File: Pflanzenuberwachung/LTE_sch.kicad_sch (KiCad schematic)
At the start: 0 parts

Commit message: Bauteile in KI CAD importiert
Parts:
- added IC1: 2615011136000, 2615011136000, symbol Bauteile:2615011136000
- added J1: Antennen Anschluss, Bauteile:Antennen Anschluss, symbol Bauteile:Antennen Anschluss
- added J2: Nano Sim, Bauteile:Nano Sim, symbol Bauteile:Nano Sim

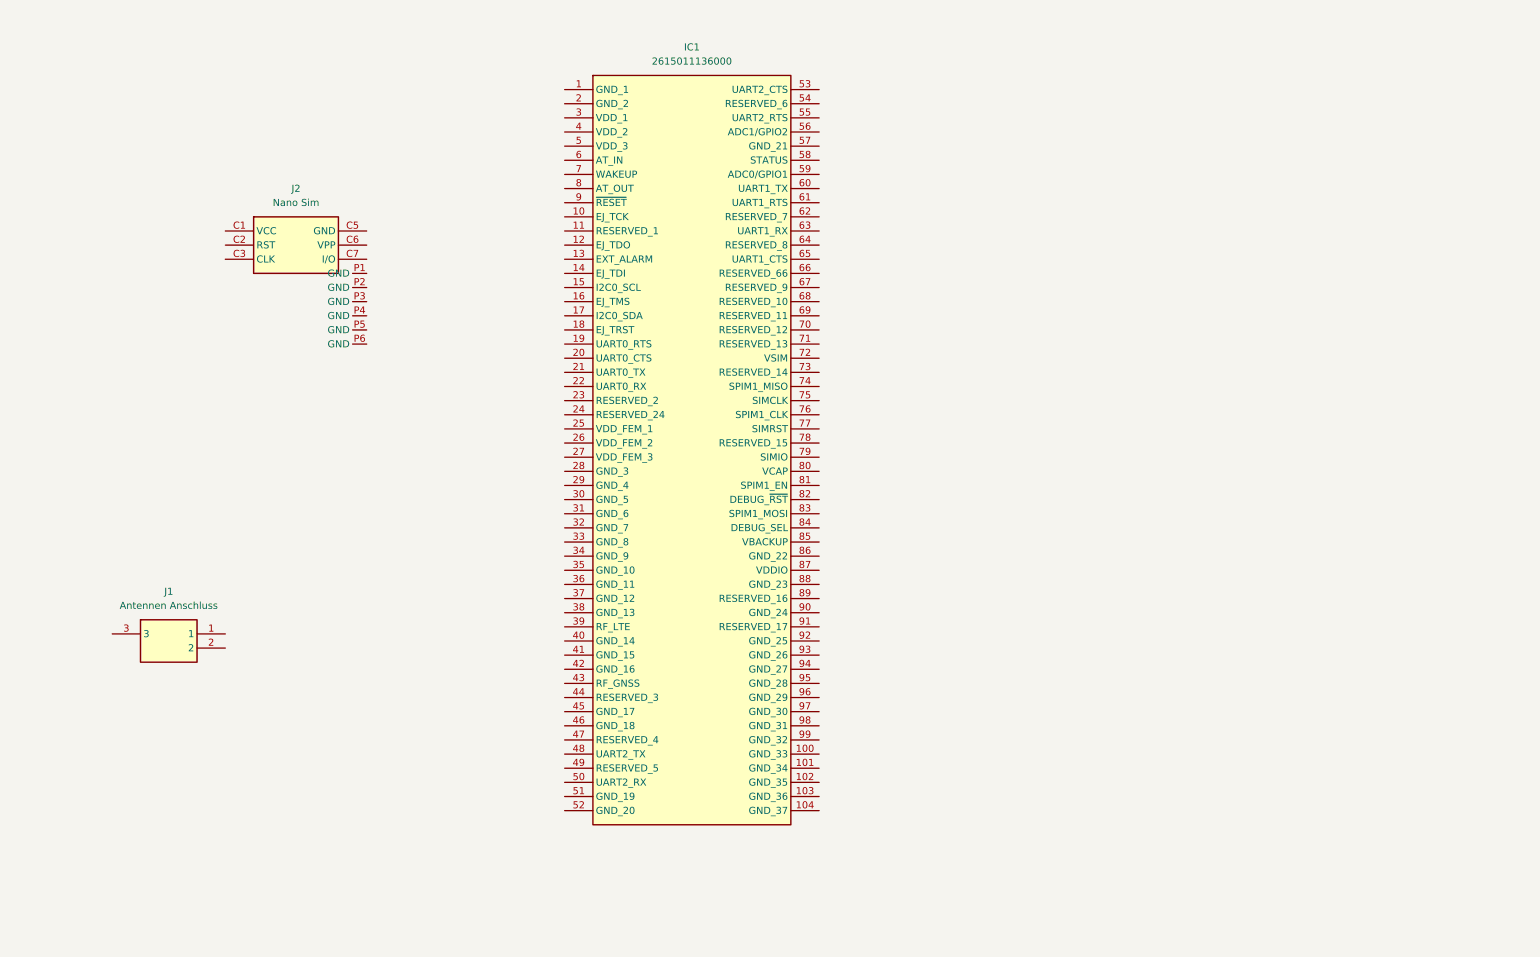
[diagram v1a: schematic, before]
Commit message: LTE und Sensoren
LTE modul und Ausgänge für Sensoren hinzugefügt
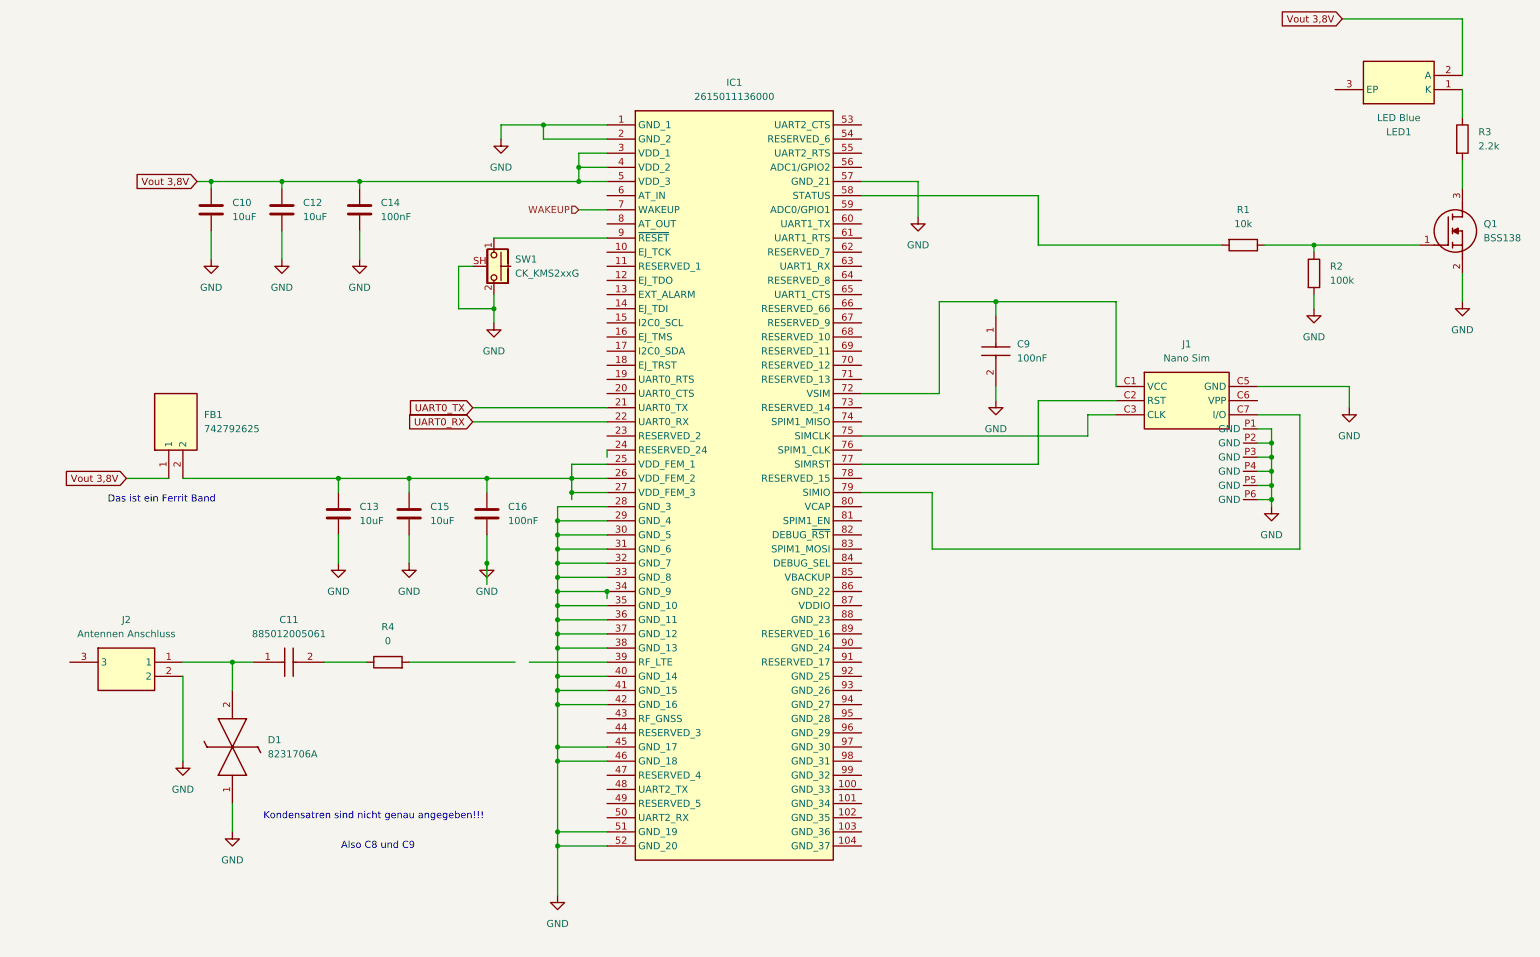
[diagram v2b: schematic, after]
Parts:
- removed J1: Antennen Anschluss, Bauteile:Antennen Anschluss, symbol Bauteile:Antennen Anschluss
- removed J2: Nano Sim, Bauteile:Nano Sim, symbol Bauteile:Nano Sim
- added C10, C12, C13, C15: 10uF, Capacitor_SMD:C_0805_2012Metric, symbol Device:C
- added C11: 885012005061, CAPC1005X55N, symbol Bauteile2:885012005061
- added C14, C16: 100nF, Capacitor_SMD:C_0805_2012Metric, symbol Device:C
- added C9: 100nF, Capacitor_SMD:C_0805_2012Metric, symbol Bauteile2:885012205037
- added D1: 8231706A, DIONC1005X60N, symbol Bauteile2:8231706A
- added FB1: 742792625, BEADC1608X100N, symbol Bauteile2:742792625
- added J1: Nano Sim, Bauteile:Nano Sim, symbol Bauteile:Nano Sim
- added J2: Antennen Anschluss, Bauteile:Antennen Anschluss, symbol Bauteile:Antennen Anschluss
- added LED1: LED Blue, Bauteile:LED Blue, symbol Bauteile:LED Blue
- added Q1: BSS138, Bauteile:Mosfed BSS138, symbol Bauteile:BSS138
- added R1: 10k, Resistor_SMD:R_0805_2012Metric, symbol Device:R
- added R2: 100k, Resistor_SMD:R_0805_2012Metric, symbol Device:R
- added R3: 2.2k, Resistor_SMD:R_0805_2012Metric, symbol Device:R
- added R4: 0, Resistor_SMD:R_0805_2012Metric, symbol Device:R
- added SW1: CK_KMS2xxG, Button_Switch_SMD:SW_SPST_CK_KMS2xxGP, symbol Switch:CK_KMS2xxG
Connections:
- net GND: now reaches IC1.1 (GND_1)
- net GND: now also IC1.2 (GND_2), IC1.28 (GND_3), IC1.29 (GND_4), IC1.30 (GND_5), IC1.31 (GND_6), IC1.32 (GND_7), IC1.33 (GND_8), IC1.34 (GND_9), IC1.35 (GND_10), IC1.36 (GND_11), IC1.37 (GND_12), IC1.38 (GND_13), IC1.40 (GND_14), IC1.41 (GND_15), IC1.42 (GND_16), IC1.45 (GND_17), IC1.46 (GND_18), IC1.51 (GND_19), IC1.52 (GND_20), IC1.57 (GND_21), C10.2, C12.2, C13.2, C14.2, C15.2, C16.2, C9.2, D1.1 (K1), J1.C5 (GND), J1.P1 (GND), J1.P2 (GND), J1.P3 (GND), J1.P4 (GND), J1.P5 (GND), J1.P6 (GND), J2.2, Q1.2 (S), R2.2, SW1.2, SW1.SH (B)
- net UART0_TX: now reaches IC1.21 (UART0_TX)
- net UART0_RX: now reaches IC1.22 (UART0_RX)
- net at IC1.25 (VDD_FEM_1): now also IC1.26 (VDD_FEM_2), IC1.27 (VDD_FEM_3), C13.1, C15.1, C16.1, FB1.2
- net Vout 3,8V: now reaches IC1.3 (VDD_1)
- net Vout 3,8V: now also IC1.4 (VDD_2), IC1.5 (VDD_3), C10.1, C12.1, C14.1, FB1.1, LED1.2 (A)
- net at IC1.58 (STATUS): now also R1.2
- net WAKEUP: now reaches IC1.7 (WAKEUP)
- net at IC1.72 (VSIM): now also C9.1, J1.C1 (VCC)
- net at IC1.75 (SIMCLK): now also J1.C3 (CLK)
- net at IC1.77 (SIMRST): now also J1.C2 (RST)
- net at IC1.79 (SIMIO): now also J1.C7 (I/O)
- net at IC1.9 (~{RESET}): now also SW1.1
- new net: Q1.1 (G), R1.1, R2.1
- new net: Q1.3 (D), R3.2
- new net: C11.1, D1.2 (K2), J2.1
- new net: LED1.1 (K), R3.1
- new net: C11.2, R4.1
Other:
- note added: "Also C8 und C9"
- note added: "Das ist ein Ferrit Band"
- note added: "Kondensatren sind nicht genau angegeben!!!"

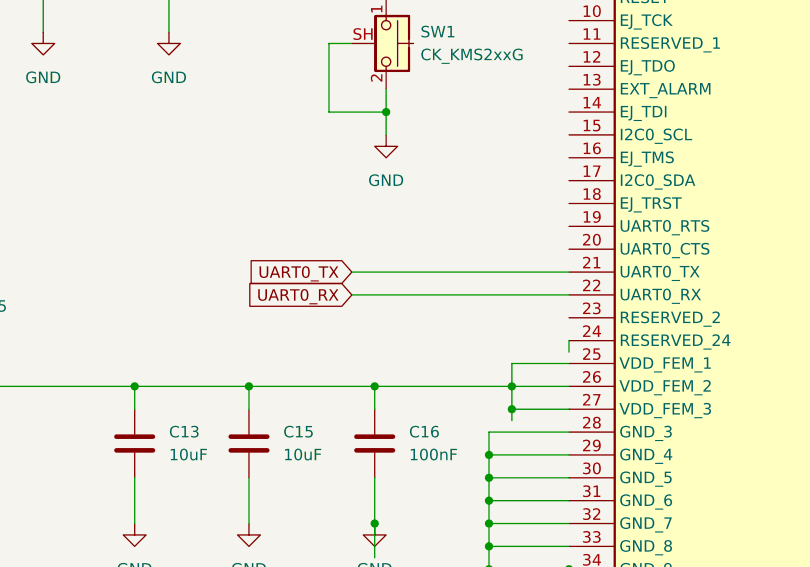
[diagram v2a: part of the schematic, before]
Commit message: Verbindungen hinzugefügt
Microprozessor mit LTE modul  und Sensoren verbungen. Plus Statusleuchte Spannungsversorgung hinzugefügt
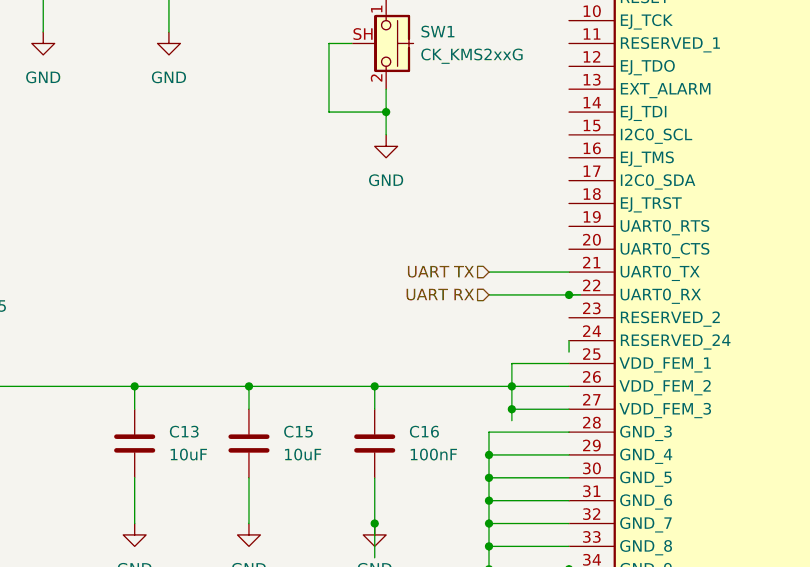
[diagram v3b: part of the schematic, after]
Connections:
- net UART0_RX renamed UART RX
- net UART0_TX renamed UART TX
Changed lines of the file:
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@@
+	)
+	(junction
+		(at 119.38 88.9)
+		(diameter 0)
+		(color 0 0 0 0)
 	)
 	(junction
@@
 	(wire
 		(pts
+			(xy 110.49 88.9) (xy 119.38 88.9)
+		)
+		(stroke
+			(width 0)
+			(type default)
+		)
+	)
+	(wire
+		(pts
 			(xy 196.85 85.09) (xy 210.82 85.09)
 		)
@@
 	(wire
 		(pts
-			(xy 95.25 88.9) (xy 119.38 88.9)
-		)
-		(stroke
-			(width 0)
-			(type default)
-		)
-	)
-	(wire
-		(pts
 			(xy 177.8 111.76) (xy 243.84 111.76)
 		)
@@
 	(wire
 		(pts
-			(xy 95.25 86.36) (xy 119.38 86.36)
-		)
-		(stroke
-			(width 0)
-			(type default)
-		)
-	)
-	(wire
-		(pts
 			(xy 60.96 45.72) (xy 60.96 46.99)
 		)
@@
 	(wire
 		(pts
+			(xy 110.49 86.36) (xy 119.38 86.36)
+		)
+		(stroke
+			(width 0)
+			(type default)
+		)
+	)
+	(wire
+		(pts
 			(xy 243.84 111.76) (xy 243.84 87.63)
 		)
@@
 		(pts
 			(xy 74.93 46.99) (xy 74.93 45.72)
+		)
+		(stroke
+			(width 0)
+			(type default)
+		)
+	)
+	(wire
+		(pts
+			(xy 119.38 88.9) (xy 120.65 88.9)
 		)
 		(stroke
@@
 			(font
 				(size 1.27 1.27)
-			)
-		)
-	)
-	(global_label "UART0_TX"
-		(shape input)
-		(at 95.25 86.36 180)
-		(fields_autoplaced yes)
-		(effects
-			(font
-				(size 1.27 1.27)
-			)
-			(justify right)
-		)
-		(property "Intersheetrefs" "${INTERSHEET_REFS}"
-			(at 83.2539 86.36 0)
-			(effects
-				(font
-					(size 1.27 1.27)
-				)
-				(justify right)
-				(hide yes)
 			)
 		)
@@
 		)
 	)
-	(global_label "UART0_RX"
-		(shape input)
-		(at 95.25 88.9 180)
-		(fields_autoplaced yes)
-		(effects
-			(font
-				(size 1.27 1.27)
-			)
-			(justify right)
-		)
-		(property "Intersheetrefs" "${INTERSHEET_REFS}"
-			(at 82.9515 88.9 0)
-			(effects
-				(font
-					(size 1.27 1.27)
-				)
-				(justify right)
-				(hide yes)
-			)
-		)
-	)
 	(global_label "Vout 3,8V"
 		(shape input)
@@
 		(fields_autoplaced yes)
 		(effects
+			(font
+				(size 1.27 1.27)
+			)
+			(justify right)
+		)
+	)
+	(hierarchical_label "UART RX"
+		(shape input)
+		(at 110.49 88.9 180)
+		(fields_autoplaced yes)
+		(effects
+			(font
+				(size 1.27 1.27)
+			)
+			(justify right)
+		)
+	)
+	(hierarchical_label "UART TX"
+		(shape input)
+		(at 110.49 86.36 180)
+		(fields_autoplaced yes)
+		(effects

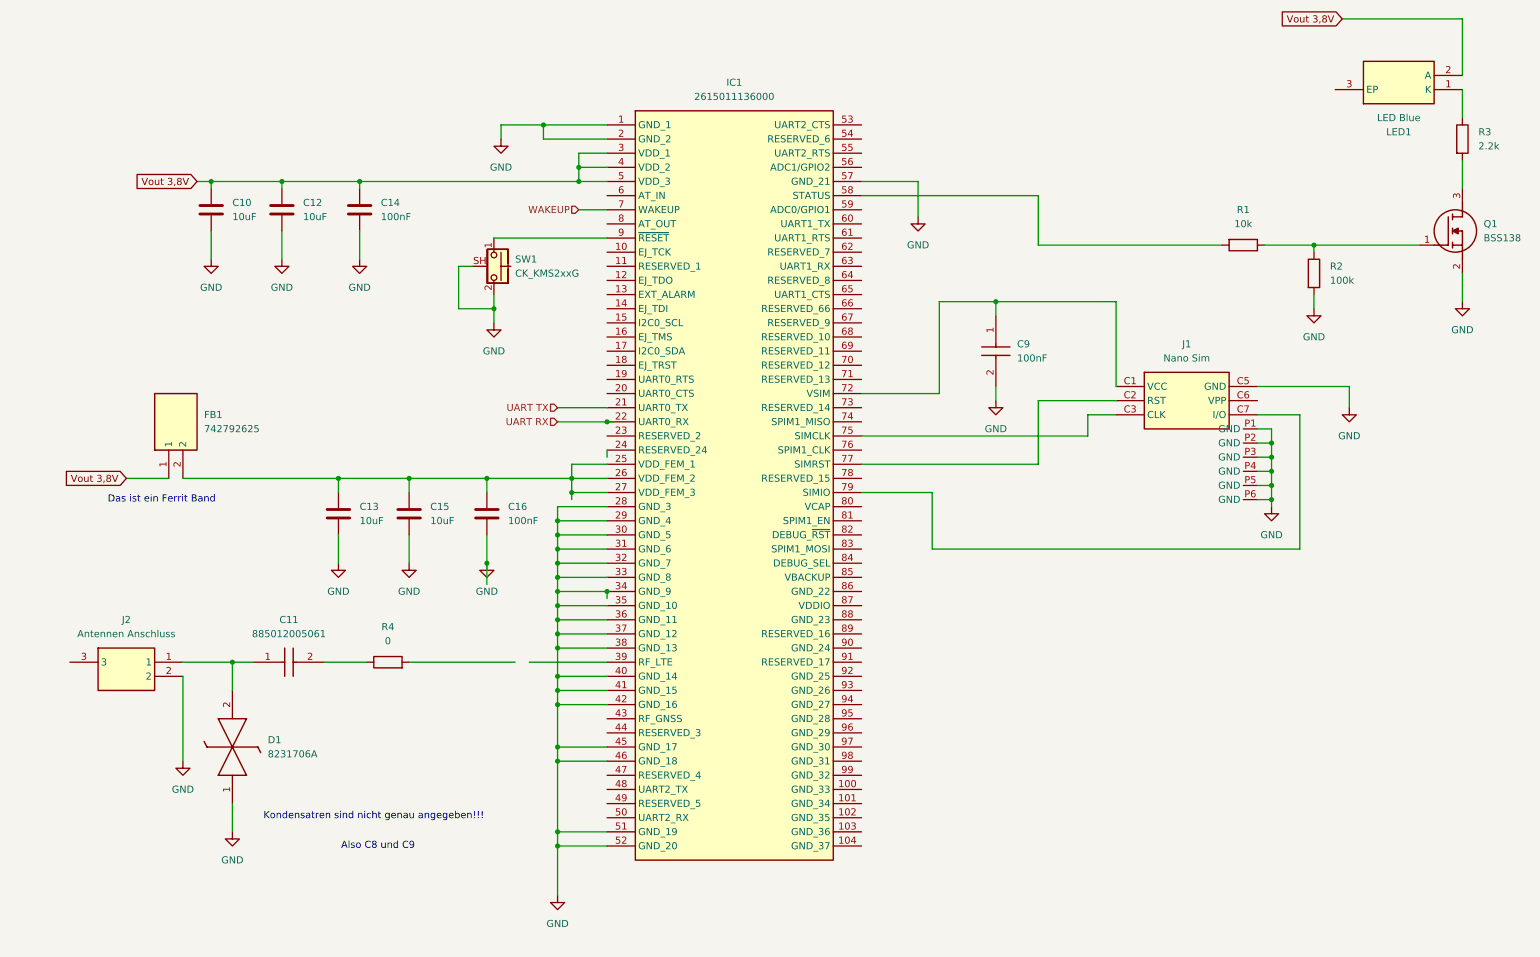
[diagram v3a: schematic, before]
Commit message: Level Shift LTE Modul für UART hinzugefügt
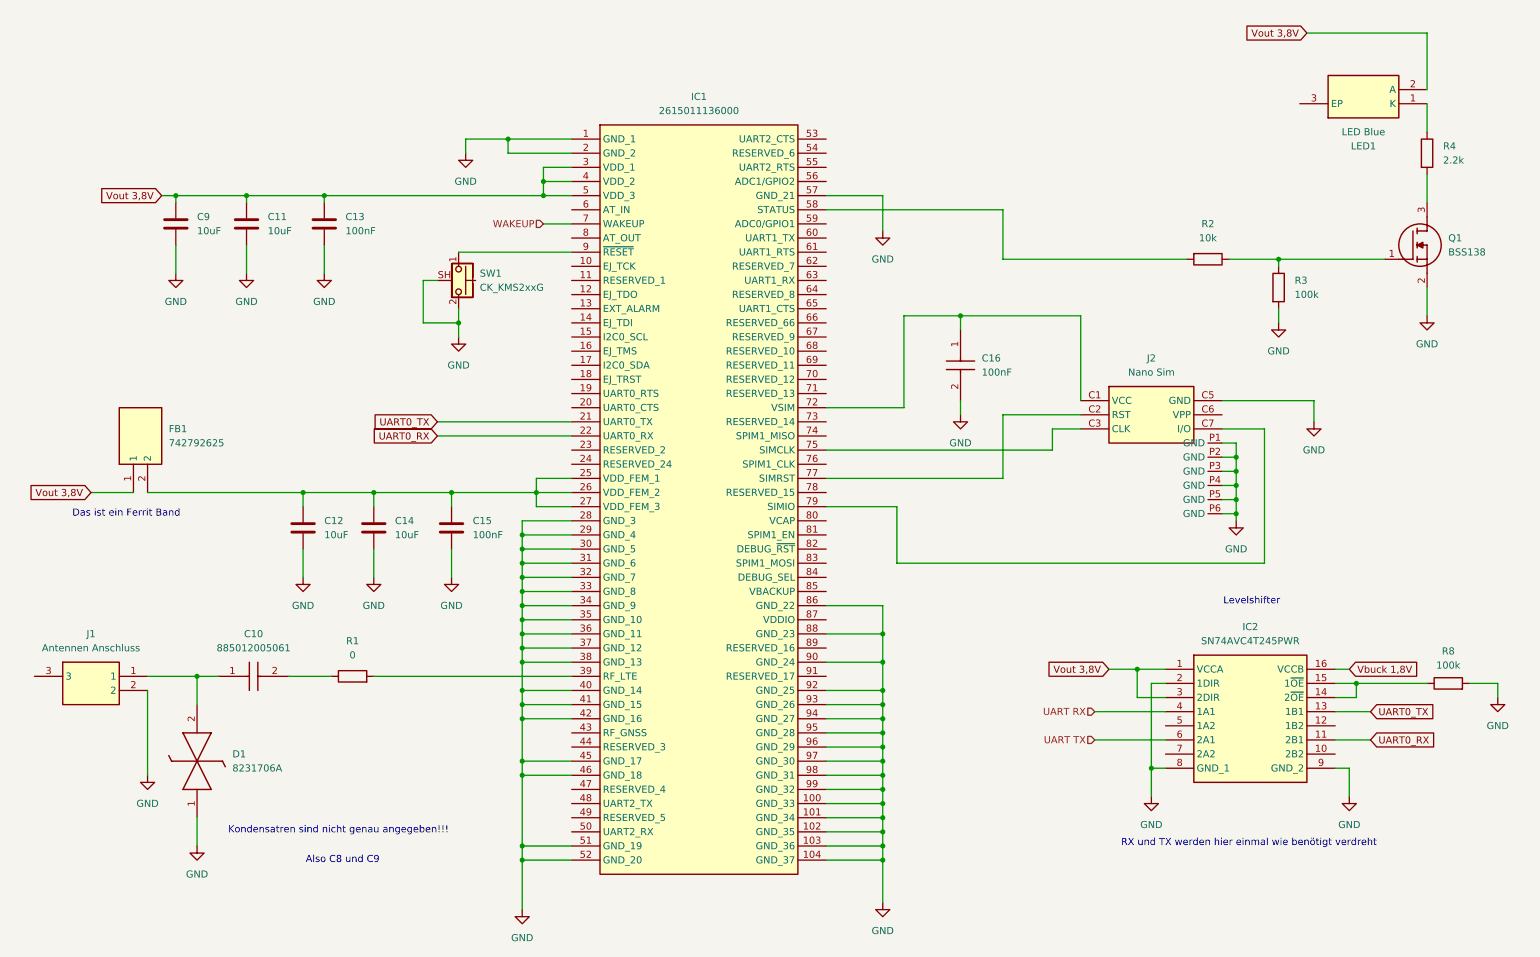
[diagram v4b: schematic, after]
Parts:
- removed C10: 10uF, Capacitor_SMD:C_0805_2012Metric, symbol Device:C
- removed C11: 885012005061, CAPC1005X55N, symbol Bauteile2:885012005061
- removed C16: 100nF, Capacitor_SMD:C_0805_2012Metric, symbol Device:C
- removed C9: 100nF, Capacitor_SMD:C_0805_2012Metric, symbol Bauteile2:885012205037
- removed J1: Nano Sim, Bauteile:Nano Sim, symbol Bauteile:Nano Sim
- removed J2: Antennen Anschluss, Bauteile:Antennen Anschluss, symbol Bauteile:Antennen Anschluss
- added C10: 885012005061, CAPC1005X55N, symbol Bauteile2:885012005061
- added C11, C9: 10uF, Capacitor_SMD:C_0805_2012Metric, symbol Device:C
- added C16: 100nF, Capacitor_SMD:C_0805_2012Metric, symbol Bauteile2:885012205037
- added IC2: SN74AVC4T245PWR, SOP65P640X120-16N, symbol Bauteile2:SN74AVC4T245PWR
- added J1: Antennen Anschluss, Bauteile:Antennen Anschluss, symbol Bauteile:Antennen Anschluss
- added J2: Nano Sim, Bauteile:Nano Sim, symbol Bauteile:Nano Sim
- added R8: 100k, Resistor_SMD:R_0805_2012Metric, symbol Device:R
- C13, C15: value 10uF -> 100nF
- C14: value 100nF -> 10uF
- R1: value 10k -> 0
- R2: value 100k -> 10k
- R3: value 2.2k -> 100k
- R4: value 0 -> 2.2k
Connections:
- net GND: now also IC1.100 (GND_33), IC1.101 (GND_34), IC1.102 (GND_35), IC1.103 (GND_36), IC1.104 (GND_37), IC1.86 (GND_22), IC1.88 (GND_23), IC1.90 (GND_24), IC1.92 (GND_25), IC1.93 (GND_26), IC1.94 (GND_27), IC1.95 (GND_28), IC1.96 (GND_29), IC1.97 (GND_30), IC1.98 (GND_31), IC1.99 (GND_32), R3.2, C11.2, C16.2, C9.2, IC2.2 (1DIR), IC2.8 (GND_1), IC2.9 (GND_2), J1.2, J2.C5 (GND), J2.P1 (GND), J2.P2 (GND), J2.P3 (GND), J2.P4 (GND), J2.P5 (GND), J2.P6 (GND), R8.2; no longer R2.2
- net UART RX: now also IC2.4 (1A1); no longer IC1.22 (UART0_RX)
- net UART TX: now also IC2.6 (2A1); no longer IC1.21 (UART0_TX)
- net Vout 3,8V: now also C13.1, C11.1, C9.1, IC2.1 (VCCA), IC2.3 (2DIR); no longer C12.1, C14.1
- net at C15.1, FB1.2, IC1.25 (VDD_FEM_1)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: now also C12.1, C14.1; no longer C13.1
- net at IC1.72 (VSIM): now also C16.1, J2.C1 (VCC)
- net at IC1.77 (SIMRST): now also J2.C2 (RST)
- net at IC1.75 (SIMCLK): now also J2.C3 (CLK)
- net at IC1.79 (SIMIO): now also J2.C7 (I/O)
- net at Q1.1 (G), R2.1: now also R3.1; no longer R1.1
- net at Q1.3 (D): now also R4.2; no longer R3.2
- net at D1.2 (K2): now also C10.1, J1.1
- net at LED1.1 (K): now also R4.1; no longer R3.1
- net at IC1.39 (RF_LTE): now also R1.2
- net at IC1.58 (STATUS): now also R2.2; no longer R1.2
- new net: C10.2, R1.1
- new net: IC2.14 (2~{OE}), IC2.15 (1~{OE}), R8.1
- new net UART0_RX: IC1.22 (UART0_RX), IC2.11 (2B1)
- new net UART0_TX: IC1.21 (UART0_TX), IC2.13 (1B1)
- new net Vbuck 1,8V: IC2.16 (VCCB)
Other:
- note added: "Levelshifter"
- note added: "RX und TX werden hier einmal wie benötigt verdreht"
